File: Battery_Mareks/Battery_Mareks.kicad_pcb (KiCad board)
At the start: 2 copper layers, 1 part

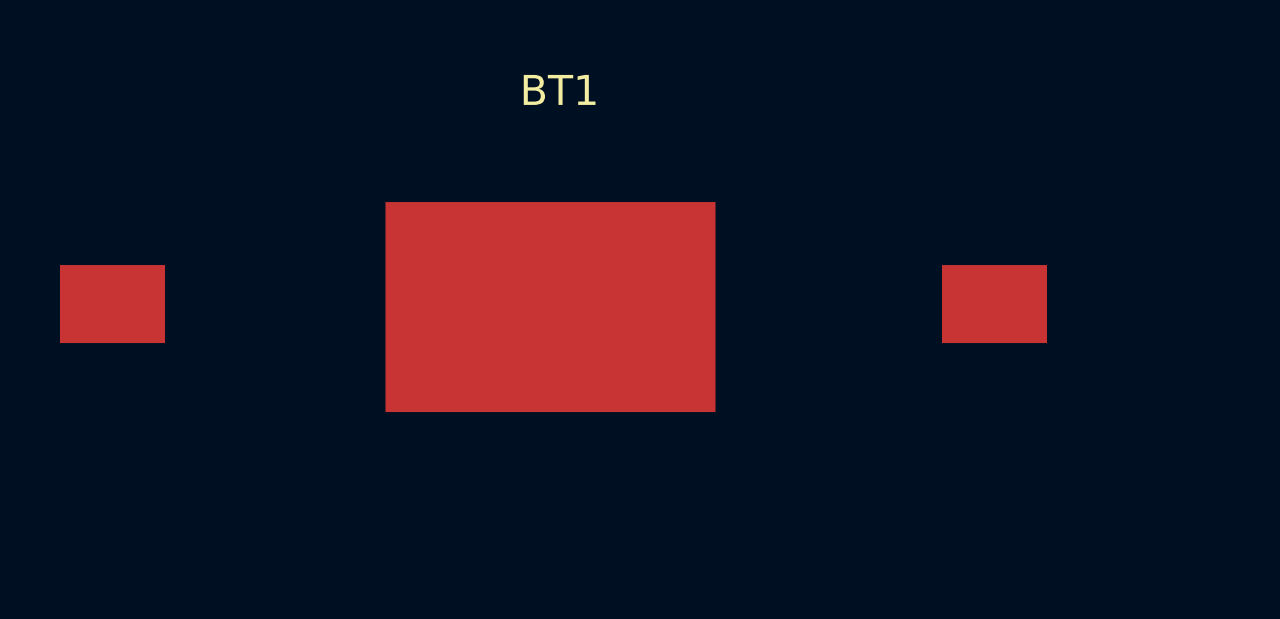
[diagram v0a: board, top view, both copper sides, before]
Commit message: 4 md par baterijām un to lodlaukumiem
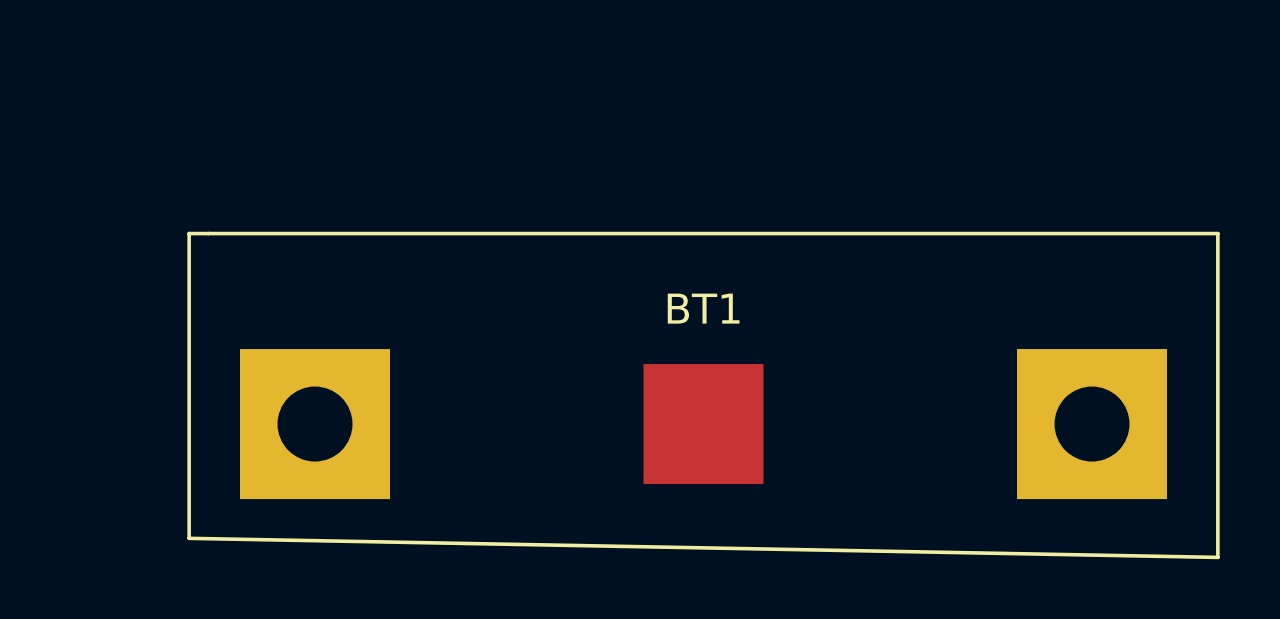
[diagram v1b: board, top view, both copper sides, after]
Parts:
- BT1: footprint Battery_Holder_:SMTU2032 -> Battery_Holder_:BC-2001
- moved BT1 6.40 mm to (115.0, 51.0)
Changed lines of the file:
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@@
     (pad_to_mask_clearance 0.05)
     (aux_axis_origin 0 0)
-    (visible_elements FFFFFF7F)
+    (visible_elements 7FFFFFFF)
     (pcbplotparams
       (layerselection 0x010fc_ffffffff)
@@
     (add_net GNDREF)
   )
-  (module Battery_Holder_:SMTU2032 (layer F.Cu)
-    (at 110 47)
-    (fp_text reference BT1 (at 0.2 -7.1) (layer F.SilkS)
+  (module Battery_Holder_:BC-2001 (layer F.Cu)
+    (at 115 51)
+    (fp_text reference BT1 (at 0 -3.81) (layer F.SilkS)
       (effects (font (size 1 1) (thickness 0.15)))
     )
-    (fp_text value Battery_Cell (at 0.05 -5.5) (layer F.Fab)
+    (fp_text value Battery_Cell (at 0 -5.08) (layer F.Fab)
       (effects (font (size 1 1) (thickness 0.15)))
     )
-    (fp_line (start -8.89 -3.81) (end -6.35 -10.795) (layer B.Paste) (width 0.12))
-    (fp_line (start -17.145 -3.81) (end -8.89 -3.81) (layer B.Paste) (width 0.12))
-    (fp_line (start -17.145 3.81) (end -17.145 -3.81) (layer B.Paste) (width 0.12))
-    (fp_line (start -8.89 3.81) (end -17.145 3.81) (layer B.Paste) (width 0.12))
-    (fp_line (start -6.35 9.525) (end -8.89 3.81) (layer B.Paste) (width 0.12))
-    (fp_line (start 8.255 -3.81) (end 5.715 -10.795) (layer B.Paste) (width 0.12))
-    (fp_line (start 17.145 -3.81) (end 8.255 -3.81) (layer B.Paste) (width 0.12))
-    (fp_line (start 17.145 3.81) (end 17.145 -3.81) (layer B.Paste) (width 0.12))
-    (fp_line (start 8.255 3.81) (end 17.145 3.81) (layer B.Paste) (width 0.12))
-    (fp_line (start 5.715 9.525) (end 8.255 3.81) (layer B.Paste) (width 0.12))
-    (fp_line (start -6.35 9.525) (end 5.715 9.525) (layer B.Paste) (width 0.12))
-    (fp_line (start -6.35 -10.795) (end 5.715 -10.795) (layer B.Paste) (width 0.12))
-    (pad 1 smd rect (at -0.1 0.1) (size 11 7) (layers F.Cu F.Paste F.Mask)
+    (fp_line (start -17.145 -6.35) (end -16.51 -6.35) (layer F.SilkS) (width 0.12))
+    (fp_line (start -17.145 3.81) (end -17.145 -6.35) (layer F.SilkS) (width 0.12))
+    (fp_line (start 17.145 4.445) (end -17.145 3.81) (layer F.SilkS) (width 0.12))
+    (fp_line (start 17.145 -6.35) (end 17.145 4.445) (layer F.SilkS) (width 0.12))
+    (fp_line (start -16.51 -6.35) (end 17.145 -6.35) (layer F.SilkS) (width 0.12))
+    (pad 1 smd rect (at 0 0) (size 4 4) (layers F.Cu F.Paste F.Mask)
       (net 1 +3V3))
-    (pad 2 smd rect (at 14.7 0) (size 3.5 2.6) (layers F.Cu F.Paste F.Mask)
+    (pad 2 thru_hole rect (at 12.95 0) (size 5 5) (drill 2.5) (layers *.Cu *.Mask)
       (net 2 GNDREF))
-    (pad 3 smd rect (at -14.7 0) (size 3.5 2.6) (layers F.Cu F.Paste F.Mask))
+    (pad 3 thru_hole rect (at -12.95 0) (size 5 5) (drill 2.5) (layers *.Cu *.Mask))
   )
 )
